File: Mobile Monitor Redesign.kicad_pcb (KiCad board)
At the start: 4 copper layers, 49 x 39.1 mm, 101 parts, among them J2 Conn_01x08_Pin, J3 Conn_01x08_Pin, J4 USB_C_Receptacle_USB2.0_16P, J7 Conn_01x05_Pin, J8 Conn_01x06_Socket, Q1 2N7002, Q2 AO3401A, Q3 BSS138, Q4 BSS138, Q5 AO3401A, Q6 2N7002, U1 ATmega2560-16A, U10 BQ27441DRZR-G1A, U11 TPL5010, U2 DS3232M, U5 XL4005, U6 IP5306, U7 CH340C, U8 FP6298XR, U9 AMS1117-3.3, Y2 Crystal

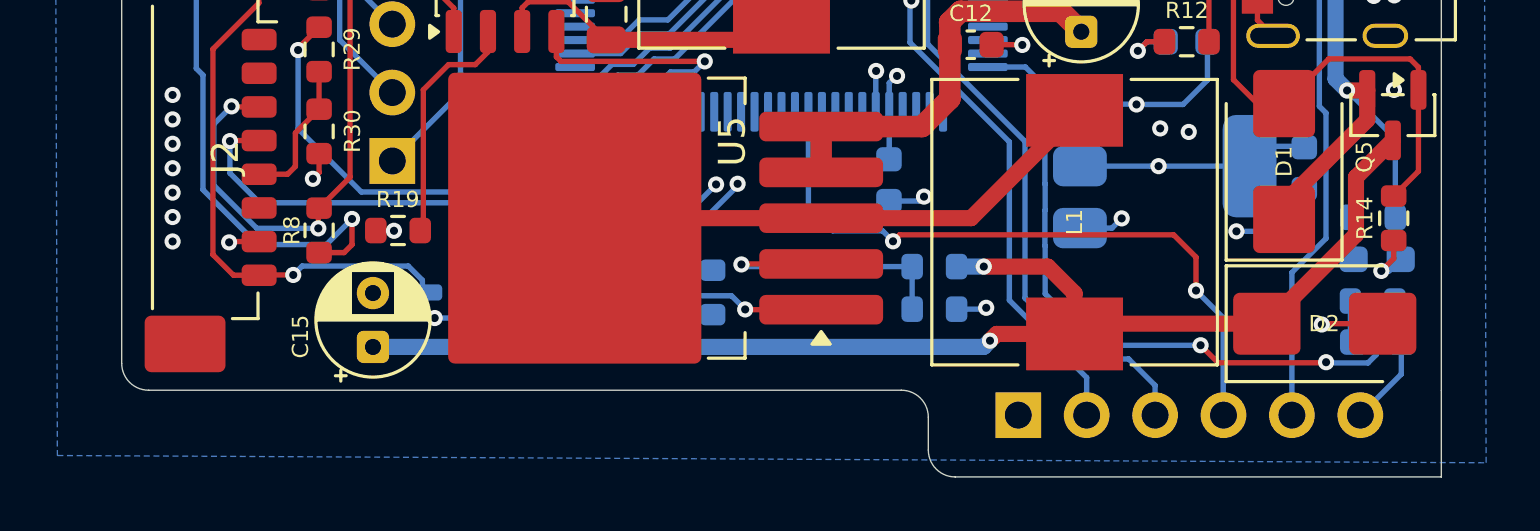
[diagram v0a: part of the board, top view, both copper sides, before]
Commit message: added another pin for power connection
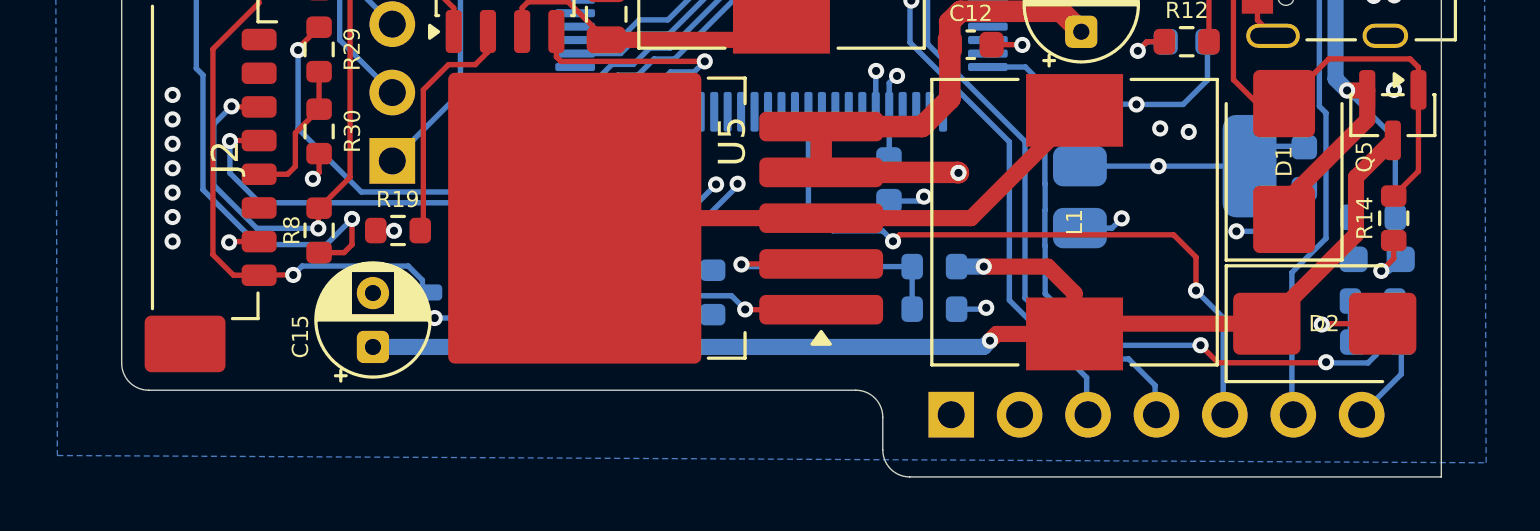
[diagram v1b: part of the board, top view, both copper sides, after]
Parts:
- removed J8: Conn_01x06_Socket, Connector_PinHeader_2.54mm:PinHeader_1x06_P2.54mm_Horizontal
- added J9: Conn_01x07_Socket, Connector_PinHeader_2.54mm:PinHeader_1x07_P2.54mm_Horizontal, B.Cu at (147.7, 118.0)
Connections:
- net /power/5:32V DC INPUT renamed 5:32V DC INPUT
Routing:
- net 5:32V DC INPUT: track 15.1 -> 29.7 mm, vias 0 -> 1
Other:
- outline, holes or cut-outs redrawn

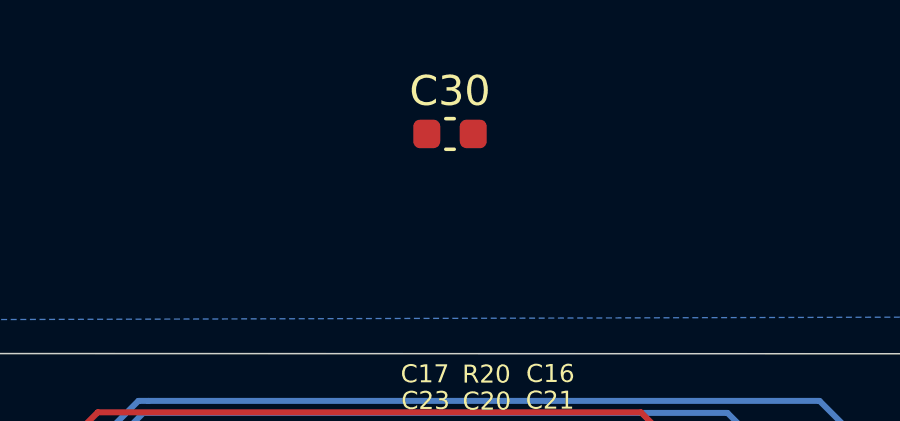
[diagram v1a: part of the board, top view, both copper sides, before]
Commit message: removed redundant SD-card schematic on base PCB
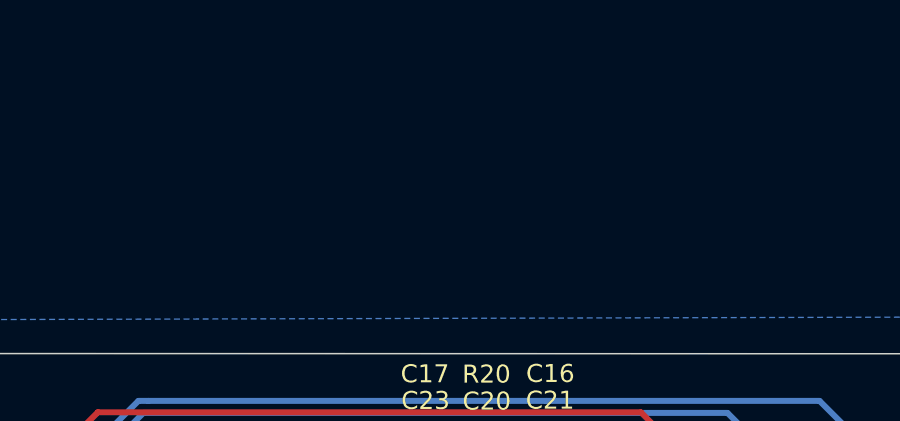
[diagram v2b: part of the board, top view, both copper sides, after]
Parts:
- removed C30: 100nF, Capacitor_SMD:C_0603_1608Metric

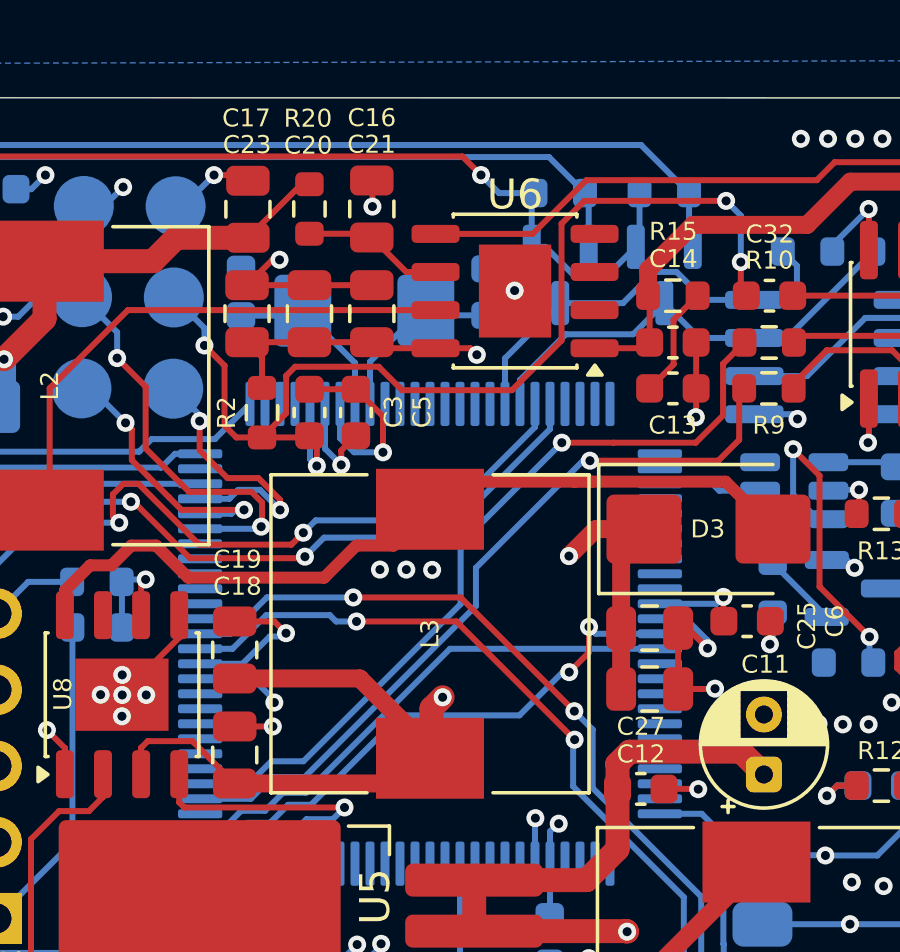
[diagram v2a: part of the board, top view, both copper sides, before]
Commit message: recheked gps serial pin mappings
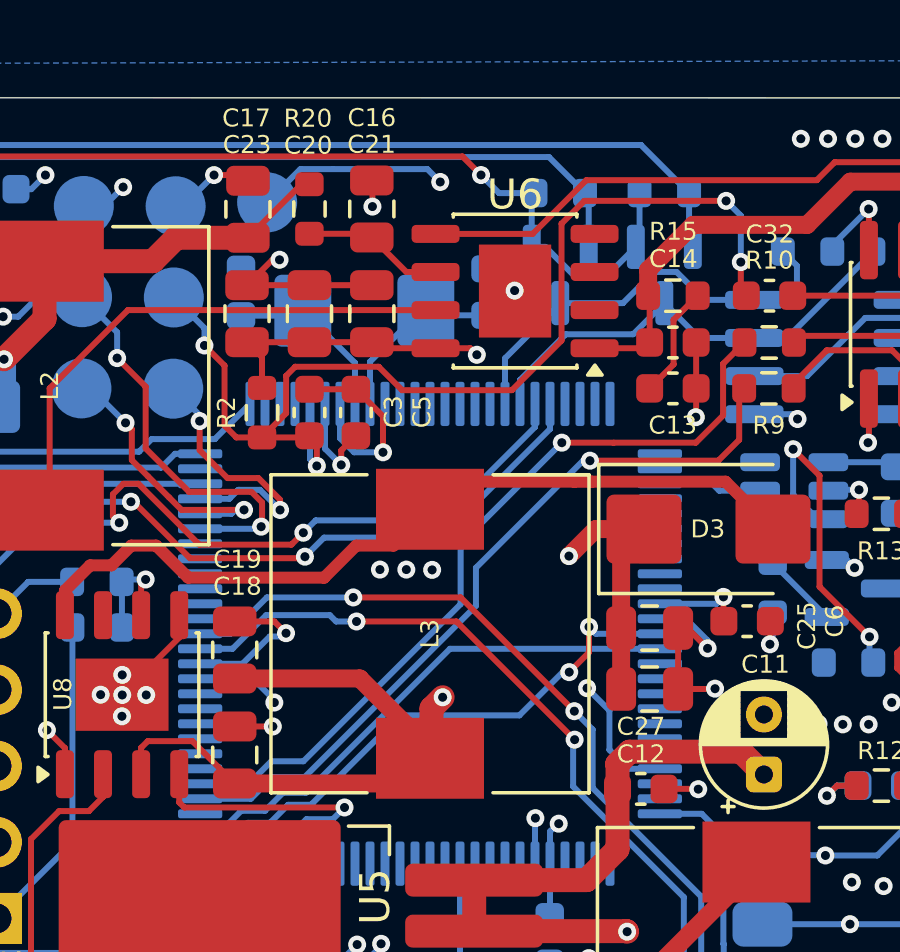
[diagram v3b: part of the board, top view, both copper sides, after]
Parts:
- added SD_CS: TestPoint_Pad_D2.0mm, TestPoint:TestPoint_Pad_D2.0mm, B.Cu at (135.9, 84.7)
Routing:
- net SD_CHIP_SELECT/D28: track 0.00 -> 33.7 mm, vias 0 -> 2
